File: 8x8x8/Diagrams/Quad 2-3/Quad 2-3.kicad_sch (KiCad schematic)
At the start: 68 parts

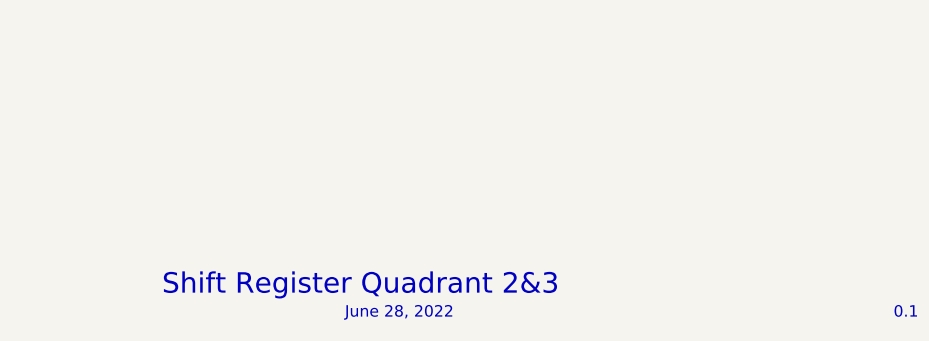
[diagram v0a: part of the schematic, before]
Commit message: revised quad 1 diagram
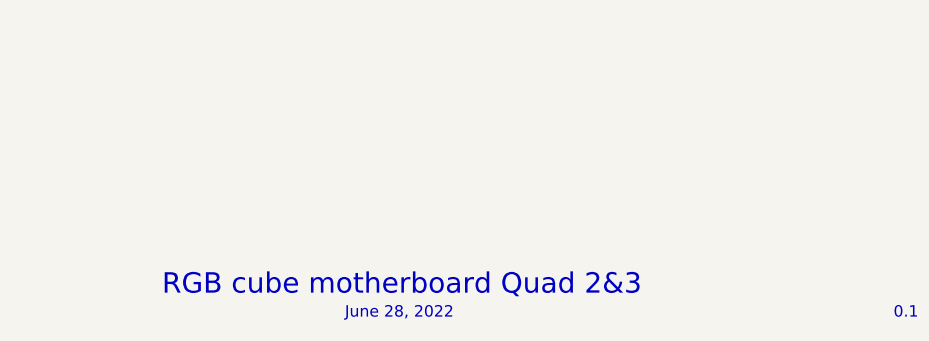
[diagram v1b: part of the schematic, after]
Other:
- note added: "RGB cube motherboard Quad 2&3"
- note removed: "Shift Register Quadrant 2&3"
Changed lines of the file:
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@@
     (effects (font (size 1.27 1.27)) (justify right bottom))
   )
-  (text "Shift Register Quadrant 2&3" (at 186.69 191.77 0)
+  (text "RGB cube motherboard Quad 2&3" (at 186.69 191.77 0)
     (effects (font (size 2.27 2.27)) (justify left bottom))
   )

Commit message: finish general layout for pcb
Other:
- note added: "RGB cube Driver Quad 2&3"
- note removed: "RGB cube motherboard Quad 2&3"
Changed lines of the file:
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@@
     (effects (font (size 1.27 1.27)) (justify right bottom))
   )
-  (text "RGB cube motherboard Quad 2&3" (at 186.69 191.77 0)
+  (text "RGB cube Driver Quad 2&3" (at 186.69 191.77 0)
     (effects (font (size 2.27 2.27)) (justify left bottom))
   )

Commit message: update
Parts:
- gave numbers to parts that had none: 68
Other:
- note added: "To next Quadrant"
- note removed: "To next Quad"
